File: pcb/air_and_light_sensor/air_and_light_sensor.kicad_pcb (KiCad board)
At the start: 2 copper layers, 48 x 21.2 mm, 4 parts, among them J10 Screw_Terminal_01x04, U3 AM2302

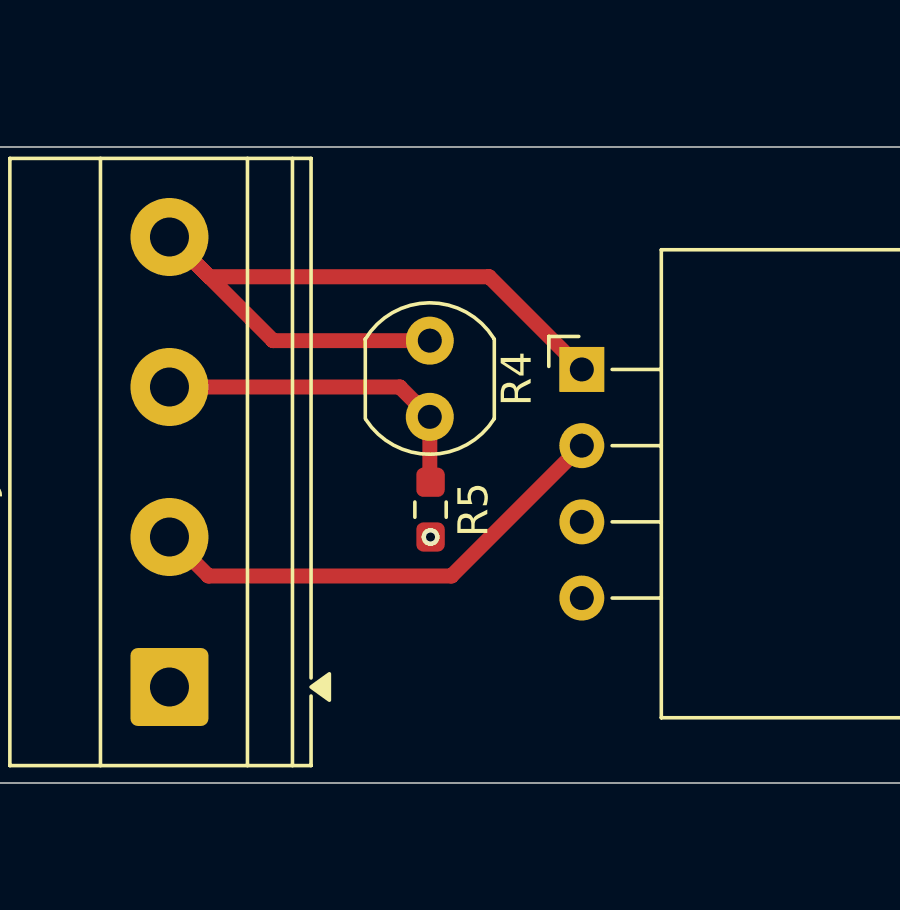
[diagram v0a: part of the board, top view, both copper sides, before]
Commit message: adding pulldown resistor to the SensorBoard
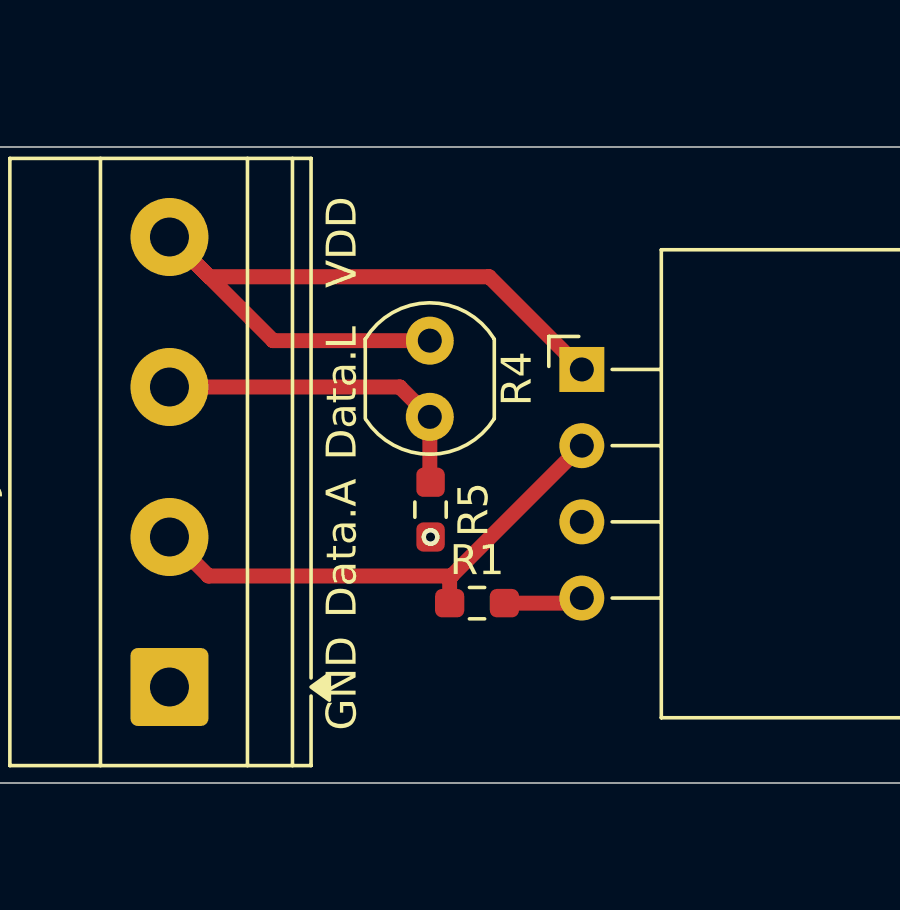
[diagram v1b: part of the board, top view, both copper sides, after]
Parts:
- added R1: 5,1k, Resistor_SMD:R_0603_1608Metric_Pad0.98x0.95mm_HandSolder, F.Cu at (91.9, 73.5)
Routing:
- net GND: track 0.00 -> 2.65 mm
- net Net-(J10-Pin_2): track 16.1 -> 17.0 mm
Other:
- board text added: "Data.A"
- board text added: "Data.L"
- board text added: "GND"
- board text added: "VDD"
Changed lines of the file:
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@@
+		)
+	)
+	(footprint "Resistor_SMD:R_0603_1608Metric_Pad0.98x0.95mm_HandSolder"
+		(layer "F.Cu")
+		(at 91.925 73.505)
+		(descr "Resistor SMD 0603 (1608 Metric), square (rectangular) end terminal, IPC-7351 nominal with elongated pad for handsoldering. (Body size source: IPC-SM-782 page 72, https://www.pcb-3d.com/wordpress/wp-content/uploads/ipc-sm-782a_amendment_1_and_2.pdf)")
+		(tags "resistor handsolder")
+		(property "Reference" "R1"
+			(at 0 -1.43 0)
+			(layer "F.SilkS")
+			(effects
+				(font
+					(size 1 1)
+					(thickness 0.15)
+				)
+			)
+		)
+		(property "Value" "5,1k"
+			(at 0 1.43 0)
+			(layer "F.Fab")
+			(effects
+				(font
+					(size 1 1)
+					(thickness 0.15)
+				)
+			)
+		)
+		(property "Datasheet" ""
+			(at 0 0 0)
+			(layer "F.Fab")
+			(hide yes)
+			(effects
+				(font
+					(size 1.27 1.27)
+				)
+			)
+		)
+		(property "Description" "Resistor"
+			(at 0 0 0)
+			(layer "F.Fab")
+			(hide yes)
+			(effects
+				(font
+					(size 1.27 1.27)
+				)
+			)
+		)
+		(property "KiLib_Generator" "SMD_2terminal_chip_molded"
+			(at 0 0 0)
+			(layer "F.SilkS")
+			(hide yes)
+			(effects
+				(font
+					(size 1 1)
+					(thickness 0.15)
+				)
+			)
+		)
+		(property ki_fp_filters "R_*")
+		(sheetname "/")
+		(sheetfile "air_and_light_sensor.kicad_sch")
+		(units
+			(unit
+				(name "A")
+				(pins "1" "2")
+			)
+		)
+		(attr smd)
+		(duplicate_pad_numbers_are_jumpers no)
+		(fp_line
+			(start -0.254724 -0.5225)
+			(end 0.254724 -0.5225)
+			(stroke
+				(width 0.12)
+				(type solid)
+			)
+			(layer "F.SilkS")
+		)
+		(fp_line
+			(start -0.254724 0.5225)
+			(end 0.254724 0.5225)
+			(stroke
+				(width 0.12)
+				(type solid)
+			)
+			(layer "F.SilkS")
+		)
+		(fp_rect
+			(start -1.65 -0.73)
+			(end 1.65 0.73)
+			(stroke
+				(width 0.05)
+				(type solid)
+			)
+			(fill no)
+			(layer "F.CrtYd")
+		)
+		(fp_rect
+			(start -0.8 -0.4125)
+			(end 0.8 0.4125)
+			(stroke
+				(width 0.1)
+				(type solid)
+			)
+			(fill no)
+			(layer "F.Fab")
+		)
+		(fp_text user "${REFERENCE}"
+			(at 0 0 0)
+			(layer "F.Fab")
+			(effects
+				(font
+					(size 0.4 0.4)
+					(thickness 0.06)
+				)
+			)
+		)
+		(pad "1" smd roundrect
+			(at -0.9125 0)
+			(size 0.975 0.95)
+			(layers "F.Cu" "F.Mask" "F.Paste")
+			(roundrect_rratio 0.25)
+			(net "Net-(J10-Pin_2)")
+			(pintype "passive")
+		)
+		(pad "2" smd roundrect
+			(at 0.9125 0)
+			(size 0.975 0.95)
+			(layers "F.Cu" "F.Mask" "F.Paste")
+			(roundrect_rratio 0.25)
+			(net "GND")
+			(pintype "passive")
+		)
+		(embedded_fonts no)
+		(model "${KICAD10_3DMODEL_DIR}/Resistor_SMD.3dshapes/R_0603_1608Metric.step"
+			(offset
+				(xyz 0 0 0)
+			)
+			(scale
+				(xyz 1 1 1)
+			)
+			(rotate
+				(xyz 0 0 0)
+			)
 		)
 	)
@@
 		(layer "Edge.Cuts")
 	)
+	(gr_text "VDD"
+		(at 88 63 90)
+		(layer "F.SilkS")
+		(effects
+			(font
+				(size 1 1)
+				(thickness 0.1)
+			)
+			(justify left bottom)
+		)
+	)
+	(gr_text "Data.L"
+		(at 88 68.745 90)
+		(layer "F.SilkS")
+		(effects
+			(font
+				(size 1 1)
+				(thickness 0.1)
+			)
+			(justify left bottom)
+		)
+	)
+	(gr_text "Data.A"
+		(at 88 74 90)
+		(layer "F.SilkS")
+		(effects
+			(font
+				(size 1 1)
+				(thickness 0.1)
+			)
+			(justify left bottom)
+		)
+	)
+	(gr_text "GND"
+		(at 88 77.75 90)
+		(layer "F.SilkS")
+		(effects
+			(font
+				(size 1 1)
+				(thickness 0.1)
+			)
+			(justify left bottom)
+		)
+	)
 	(segment
 		(start 90.35 67.295)
@@
 	)
 	(segment
-		(start 82.9975 62.625)
-		(end 92.3275 62.625)
-		(width 0.5)
-		(layer "F.Cu")
-		(net "VDD")
-	)
-	(segment
-		(start 85.1275 64.755)
-		(end 90.35 64.755)
-		(width 0.5)
-		(layer "F.Cu")
-		(net "VDD")
-	)
-	(segment
-		(start 92.3275 62.625)
-		(end 95.4175 65.715)
-		(width 0.5)
-		(layer "F.Cu")
-		(net "VDD")
-	)
-	(segment
-		(start 81.6725 61.3)
-		(end 82.9975 62.625)
-		(width 0.5)
-		(layer "F.Cu")
-		(net "VDD")
-	)
-	(segment
-		(start 81.6725 61.3)
-		(end 85.1275 64.755)
-		(width 0.5)
-		(layer "F.Cu")
-		(net "VDD")
-	)
-	(segment
-		(start 91.0725 72.6)
-		(end 95.4175 68.255)
-		(width 0.5)
-		(layer "F.Cu")
-		(net "Net-(J10-Pin_2)")
-	)
-	(segment
-		(start 81.6725 71.3)
-		(end 82.9725 72.6)
-		(width 0.5)
-		(layer "F.Cu")
-		(net "Net-(J10-Pin_2)")
-	)
-	(segment
-		(start 82.9725 72.6)
-		(end 91.0725 72.6)
-		(width 0.5)
-		(layer "F.Cu")
-		(net "Net-(J10-Pin_2)")
+		(start 95.2475 73.505)
+		(end 95.4175 73.335)
+		(width 0.5)
+		(layer "F.Cu")
+		(net "GND")
+	)
+	(segment
+		(start 92.8375 73.505)
+		(end 95.2475 73.505)
+		(width 0.5)
+		(layer "F.Cu")
+		(net "GND")
 	)
 	(via
@@
 		(net "GND")
 	)
+	(segment
+		(start 91.0725 72.6)
+		(end 95.4175 68.255)
+		(width 0.5)
+		(layer "F.Cu")
+		(net "Net-(J10-Pin_2)")
+	)
+	(segment
+		(start 91.0125 72.66)
+		(end 91.0725 72.6)
+		(width 0.5)
+		(layer "F.Cu")
+		(net "Net-(J10-Pin_2)")
+	)
+	(segment
+		(start 81.6725 71.3)
+		(end 82.9725 72.6)
+		(width 0.5)
+		(layer "F.Cu")
+		(net "Net-(J10-Pin_2)")
+	)
+	(segment
+		(start 82.9725 72.6)
+		(end 91.0725 72.6)
+		(width 0.5)
+		(layer "F.Cu")
+		(net "Net-(J10-Pin_2)")
+	)
+	(segment
+		(start 91.0125 73.505)
+		(end 91.0125 72.66)
+		(width 0.5)
+		(layer "F.Cu")
+		(net "Net-(J10-Pin_2)")
+	)
+	(segment
+		(start 82.9975 62.625)
+		(end 92.3275 62.625)
+		(width 0.5)
+		(layer "F.Cu")
+		(net "VDD")
+	)
+	(segment
+		(start 85.1275 64.755)
+		(end 90.35 64.755)
+		(width 0.5)
+		(layer "F.Cu")
+		(net "VDD")
+	)
+	(segment
+		(start 92.3275 62.625)
+		(end 95.4175 65.715)
+		(width 0.5)
+		(layer "F.Cu")
+		(net "VDD")
+	)
+	(segment
+		(start 81.6725 61.3)
+		(end 82.9975 62.625)
+		(width 0.5)
+		(layer "F.Cu")
+		(net "VDD")
+	)
+	(segment
+		(start 81.6725 61.3)
+		(end 85.1275 64.755)
+		(width 0.5)
+		(layer "F.Cu")
+		(net "VDD")
+	)
 	(zone

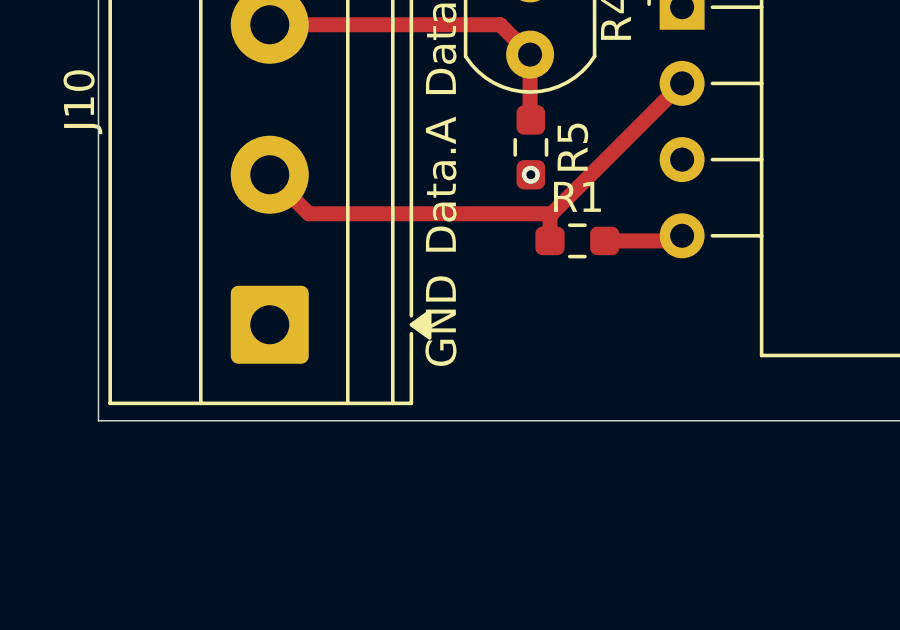
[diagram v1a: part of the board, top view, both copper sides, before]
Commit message: merging the BOMs
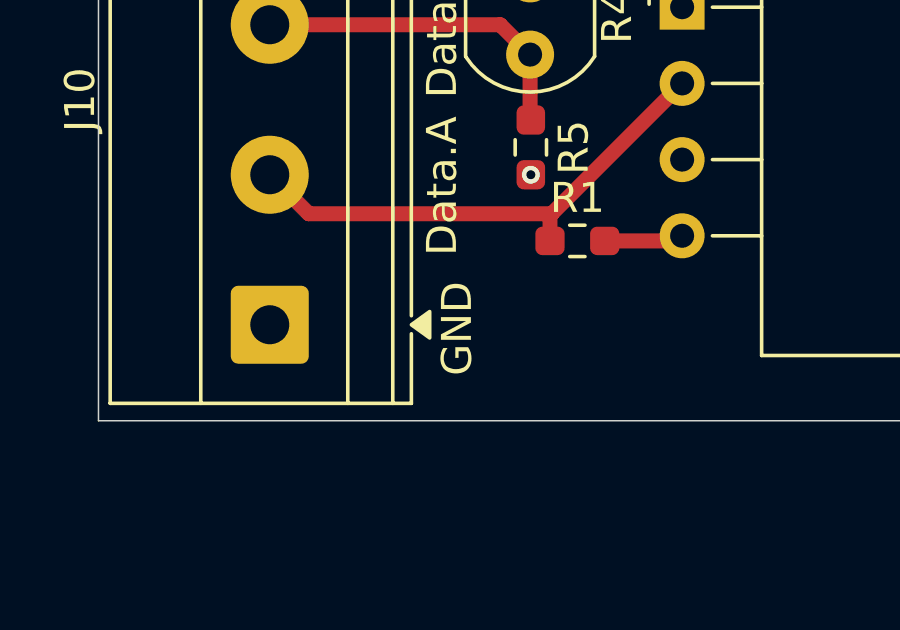
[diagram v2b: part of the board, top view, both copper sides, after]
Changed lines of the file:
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@@
 	)
 	(gr_text "GND"
-		(at 88 77.75 90)
+		(at 88.5 78 90)
 		(layer "F.SilkS")
 		(effects
